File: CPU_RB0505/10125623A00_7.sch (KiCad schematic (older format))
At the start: 71 parts, among them IC20 SN74LVC1G07DBVT, IC6 SN74LVC1G07DBVT, J1 ZIF-52610-2290, J17 FH_40BR, J3 , J6 87606-408, J7 26BR-HE10, T1 2N7002, T16 IRLML5103, T2 2N7002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

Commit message: Combined all symbols into one project library
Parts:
- C111, C17, C18, C41, C52, C55, C58: symbol 10125623A00-eagle-import:RESEAU_4C -> cpu-board:RESEAU_4C
- C19, C31, C32, C34: symbol 10125623A00-eagle-import:TANTALB -> cpu-board:TANTALB
- C35: symbol 10125623A00-eagle-import:C0805 -> cpu-board:C0805
- C87: symbol 10125623A00-eagle-import:C0603 -> cpu-board:C0603
- IC20, IC6: symbol 10125623A00-eagle-import:LVC1G07DBVT -> cpu-board:LVC1G07DBVT
- J1: symbol 10125623A00-eagle-import:ZIF-52610-2290 -> cpu-board:ZIF-52610-2290
- J17: symbol 10125623A00-eagle-import:FH_40BR -> cpu-board:FH_40BR
- J3: symbol 10125623A00-eagle-import:B12B-ZR -> cpu-board:B12B-ZR
- J6: symbol 10125623A00-eagle-import:87606-408 -> cpu-board:87606-408
- J7: symbol 10125623A00-eagle-import:26BR-HE10 -> cpu-board:26BR-HE10
- JP1: symbol 10125623A00-eagle-import:JUMP_0U -> cpu-board:JUMP_0U
- L1, L16, L18, L3, L35, L36, L38, L39, L4, L40, L41, L42, L43, L44, L45, L46, L47, L48, L49, L50, L51, L52, L53, L6: symbol 10125623A00-eagle-import:74279263 -> cpu-board:74279263
- L5, R12, R13, R20, R21, R24, R25, R26, R27, R30, R32, R47, R7: symbol 10125623A00-eagle-import:R0805 -> cpu-board:R0805
- L61, L8: symbol 10125623A00-eagle-import:7427504 -> cpu-board:7427504
- R16, R22, R23, R31: symbol 10125623A00-eagle-import:R1206 -> cpu-board:R1206
- T1, T2, T4, T5: symbol 10125623A00-eagle-import:IRLML2803 -> cpu-board:IRLML2803
- T16: symbol 10125623A00-eagle-import:IRLML5103 -> cpu-board:IRLML5103
- T8, T9: symbol 10125623A00-eagle-import:IRLML2803@2 -> cpu-board:IRLML2803@2

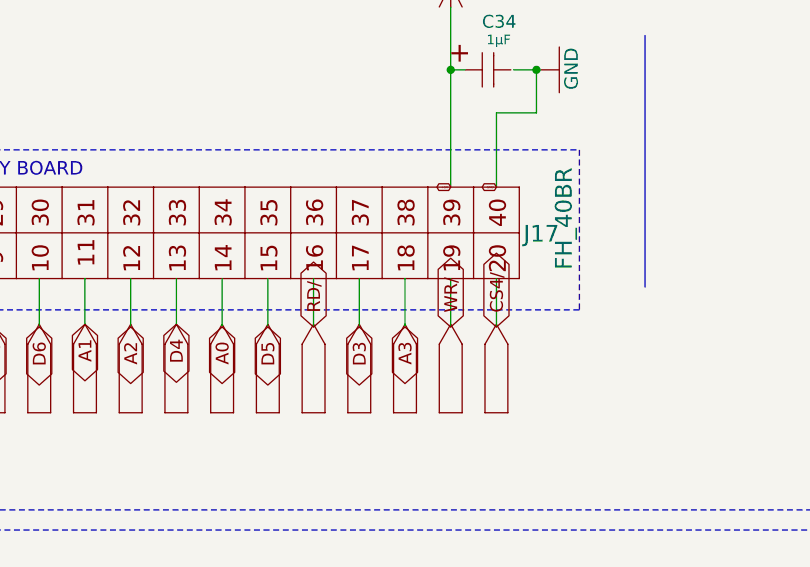
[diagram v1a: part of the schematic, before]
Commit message: Global Labels with '/' character changed to '\'
Kicad doesn't allow the former
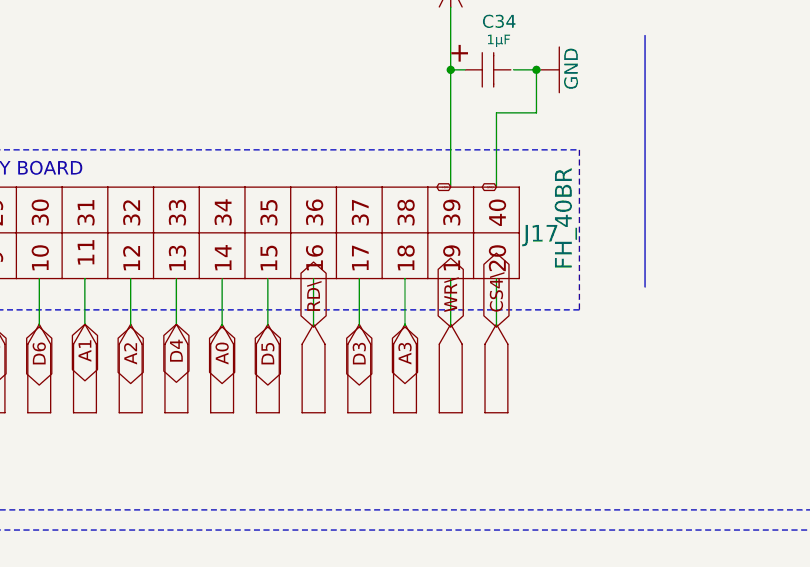
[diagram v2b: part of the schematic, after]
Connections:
- net labels added: CS4\, RD\, WR\
- net labels removed: CS4/, RD/, WR/
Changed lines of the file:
@@
 	13587 2213 13587 2425
 Text GLabel 13587 2425 1    56   BiDi ~ 0
-RD/
+RD\
 Wire Wire Line
 	14187 2213 14187 2425
 Text GLabel 14187 2425 1    56   BiDi ~ 0
-WR/
+WR\
 Wire Wire Line
 	14387 2213 14387 2425
 Text GLabel 14387 2425 1    56   BiDi ~ 0
-CS4/
+CS4\
 Wire Wire Line
 	3237 5425 3012 5425

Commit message: Sheet 7 is on-grid and pretty
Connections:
- net labels removed: PORT, PORT_COU, PORT_LONG
- wire segments 346 -> 350
- no-connect marks 0 -> 46
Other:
- moved on the sheet: C19, C31, C32, C34, J17, L35, L36, L38, L39, L40, L41, L42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

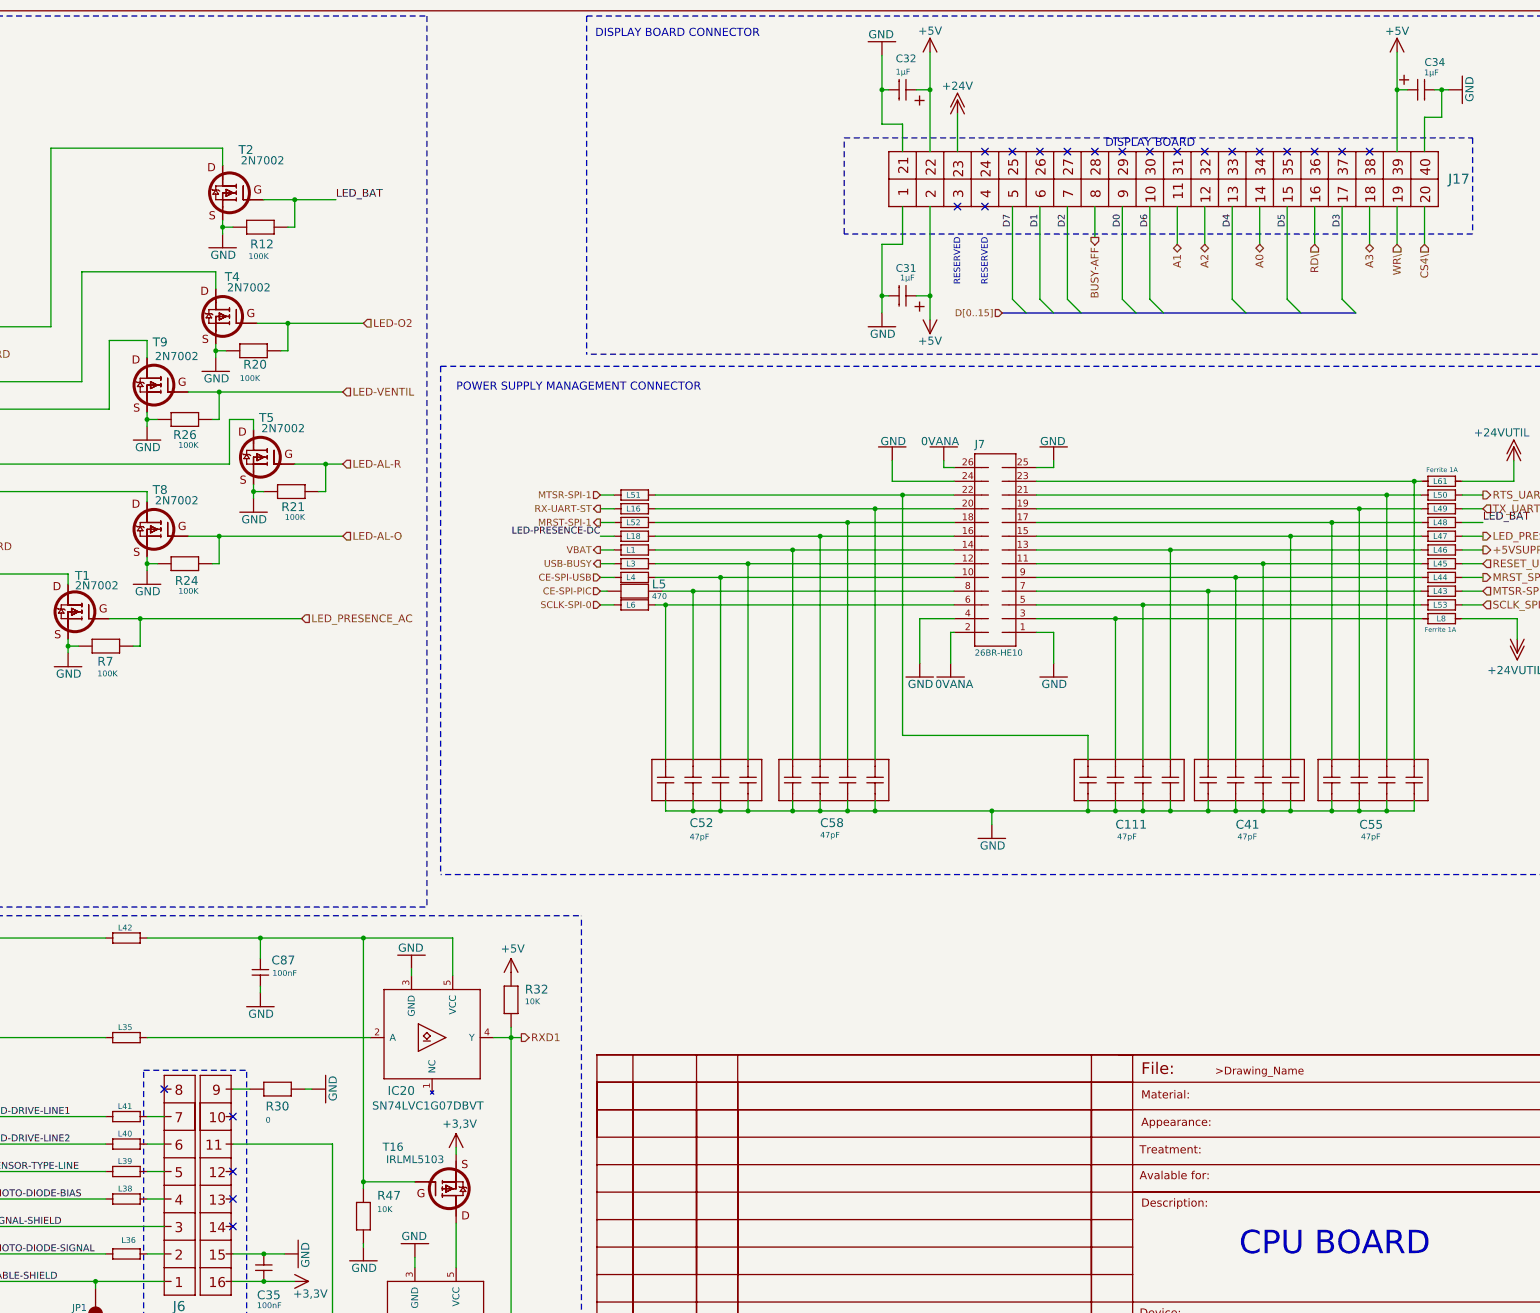
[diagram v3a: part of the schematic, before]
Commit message: Standardized value suffixes to "k" and "u"
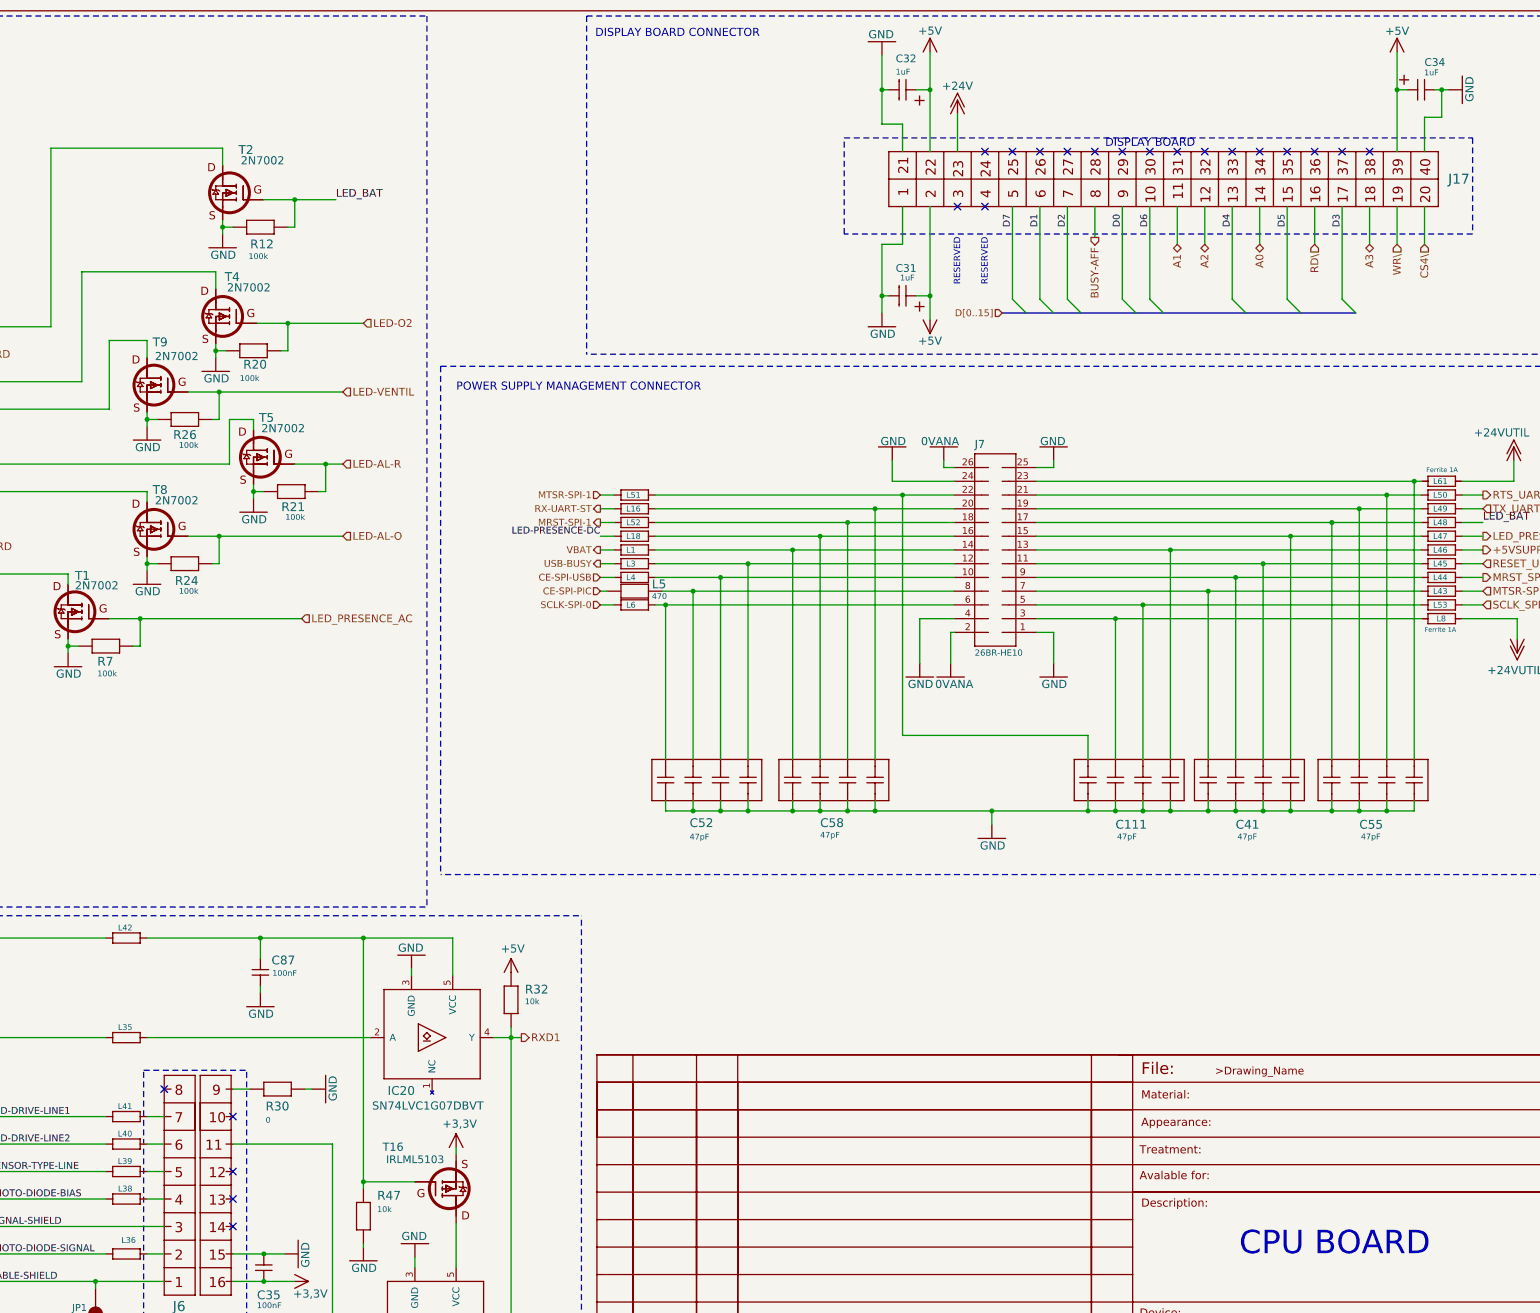
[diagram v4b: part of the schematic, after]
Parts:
- C31, C32, C34: value 1µF -> 1uF
- R12, R20, R21, R24, R26, R7: value 100K -> 100k
- R32, R47: value 10K -> 10k
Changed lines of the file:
@@
 P 5875 3200
 F 0 "R20" H 5950 3338 64  0000 R TNN
-F 1 "100K" H 5975 3425 42  0000 R TNN
+F 1 "100k" H 5975 3425 42  0000 R TNN
 F 2 "10125623A00:R0805" H 5875 3200 50  0001 C CNN
 F 3 "" H 5875 3200 50  0001 C CNN
@@
 P 6150 4225
 F 0 "R21" H 6050 4300 64  0000 L BNN
-F 1 "100K" H 6050 4387 42  0000 L BNN
+F 1 "100k" H 6050 4387 42  0000 L BNN
 F 2 "10125623A00:R0805" H 6150 4225 50  0001 C CNN
 F 3 "" H 6150 4225 50  0001 C CNN
@@
 P 5375 4750
 F 0 "R24" H 5275 4837 64  0000 L BNN
-F 1 "100K" H 5275 4925 42  0000 L BNN
+F 1 "100k" H 5275 4925 42  0000 L BNN
 F 2 "10125623A00:R0805" H 5375 4750 50  0001 C CNN
 F 3 "" H 5375 4750 50  0001 C CNN
@@
 P 5375 3700
 F 0 "R26" H 5288 3775 64  0000 L BNN
-F 1 "100K" H 5275 3863 42  0000 L BNN
+F 1 "100k" H 5275 3863 42  0000 L BNN
 F 2 "10125623A00:R0805" H 5375 3700 50  0001 C CNN
 F 3 "" H 5375 3700 50  0001 C CNN
@@
 P 10600 2800
 F 0 "C31" V 10432 2750 56  0000 L BNN
-F 1 "1µF" V 10444 2888 42  0000 R TNN
+F 1 "1uF" V 10444 2888 42  0000 R TNN
 F 2 "10125623A00:TANTALB" H 10600 2800 50  0001 C CNN
 F 3 "" H 10600 2800 50  0001 C CNN
@@
 P 10600 1300
 F 0 "C32" V 10406 1250 56  0000 L BNN
-F 1 "1µF" V 10494 1250 42  0000 L BNN
+F 1 "1uF" V 10494 1250 42  0000 L BNN
 F 2 "10125623A00:TANTALB" H 10600 1300 50  0001 C CNN
 F 3 "" H 10600 1300 50  0001 C CNN
@@
 P 7750 7925
 F 0 "R32" V 7788 7825 64  0000 R TNN
-F 1 "10K" V 7713 7825 42  0000 R TNN
+F 1 "10k" V 7713 7825 42  0000 R TNN
 F 2 "10125623A00:R0805" H 7750 7925 50  0001 C CNN
 F 3 "" H 7750 7925 50  0001 C CNN
@@
 P 4800 5350
 F 0 "R7" H 4862 5500 64  0000 R TNN
-F 1 "100K" H 4862 5575 42  0000 R TNN
+F 1 "100k" H 4862 5575 42  0000 R TNN
 F 2 "10125623A00:R0805" H 4800 5350 50  0001 C CNN
 F 3 "" H 4800 5350 50  0001 C CNN
@@
 P 5925 2300
 F 0 "R12" H 6000 2462 64  0000 R TNN
-F 1 "100K" H 6012 2537 42  0000 R TNN
+F 1 "100k" H 6012 2537 42  0000 R TNN
 F 2 "10125623A00:R0805" H 5925 2300 50  0001 C CNN
 F 3 "" H 5925 2300 50  0001 C CNN
@@
 P 6675 9500
 F 0 "R47" V 6787 9400 64  0000 R TNN
-F 1 "10K" V 6700 9400 42  0000 R TNN
+F 1 "10k" V 6700 9400 42  0000 R TNN
 F 2 "10125623A00:R0805" H 6675 9500 50  0001 C CNN
 F 3 "" H 6675 9500 50  0001 C CNN
@@
 P 14375 1300
 F 0 "C34" V 14575 1200 56  0000 C CNN
-F 1 "1µF" V 14500 1225 42  0000 C CNN
+F 1 "1uF" V 14500 1225 42  0000 C CNN
 F 2 "10125623A00:TANTALB" H 14375 1300 50  0001 C CNN
 F 3 "" H 14375 1300 50  0001 C CNN

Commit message: Updated to 'default.kicad_wks' - deleted sheet symbol - general cleanup
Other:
- note removed: "10125623"
- note removed: "CPU BOARD"
- note removed: "RB0505"
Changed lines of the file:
@@
 encoding utf-8
 Sheet 8 8
-Title ""
+Title "RB0505 CPU Board"
 Date ""
 Rev ""
@@
 $EndComp
 $Comp
-L cpu-board:CART_A3 #U$544
-U 1 1 AC16480B
-P 875 11125
-F 0 "#U$544" H 875 11125 50  0001 C CNN
-F 1 "CART_A3" H 875 11125 50  0001 C CNN
-F 2 "" H 875 11125 50  0001 C CNN
-F 3 "" H 875 11125 50  0001 C CNN
-	1    875  11125
-	1    0    0    -1
-$EndComp
-$Comp
 L cpu-board:GND #U$547
 U 1 1 7F698F3F
@@
 Text Notes 950  2200 0    56   ~ 0
 BOTTOM(-)
-Text Notes 13050 9800 0    170  ~ 0
-CPU BOARD
-Text Notes 13500 10550 0    170  ~ 0
-RB0505
-Text Notes 13775 11025 0    170  ~ 0
-10125623
-Text Notes 8375 10638 0    59   ~ 0
+Text Notes 15825 10788 0    59   ~ 0
 A
-Text Notes 8650 10638 0    59   ~ 0
+Text Notes 16100 10788 0    59   ~ 0
 05/03/14
-Text Notes 9150 10650 0    59   ~ 0
+Text Notes 16600 10800 0    59   ~ 0
 JR
 Text Notes 1350 8188 0    47   ~ 0

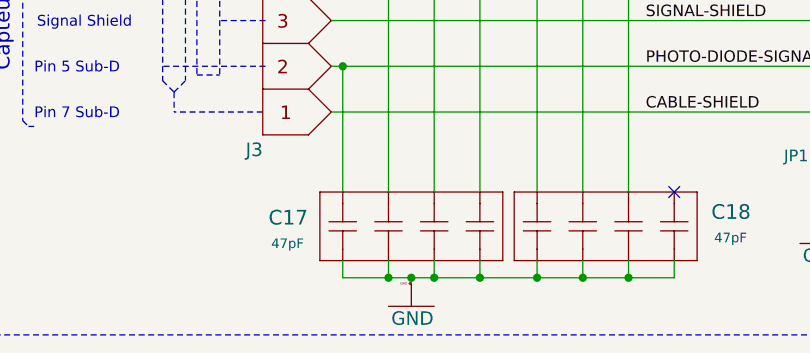
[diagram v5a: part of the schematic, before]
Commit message: All hierarchical labels placed on top sheet
And removed redundant labels and minor issues corrected here and there.
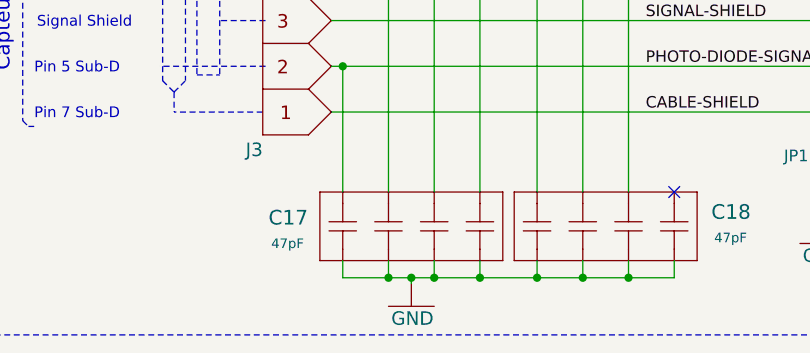
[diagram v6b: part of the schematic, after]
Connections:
- net GND: no longer names the net of C17.1, C17.2, C17.3, C17.4, C18.1, C18.2, C18.3, C18.4
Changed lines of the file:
@@
 Connection ~ 3675 10700
 Connection ~ 3875 10700
-Text HLabel 2925 10725 0    10   BiDi ~ 0
-GND
 Wire Wire Line
 	6675 9700 6675 9725
